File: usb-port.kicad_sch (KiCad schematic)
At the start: 6 parts, among them J3 USB_A

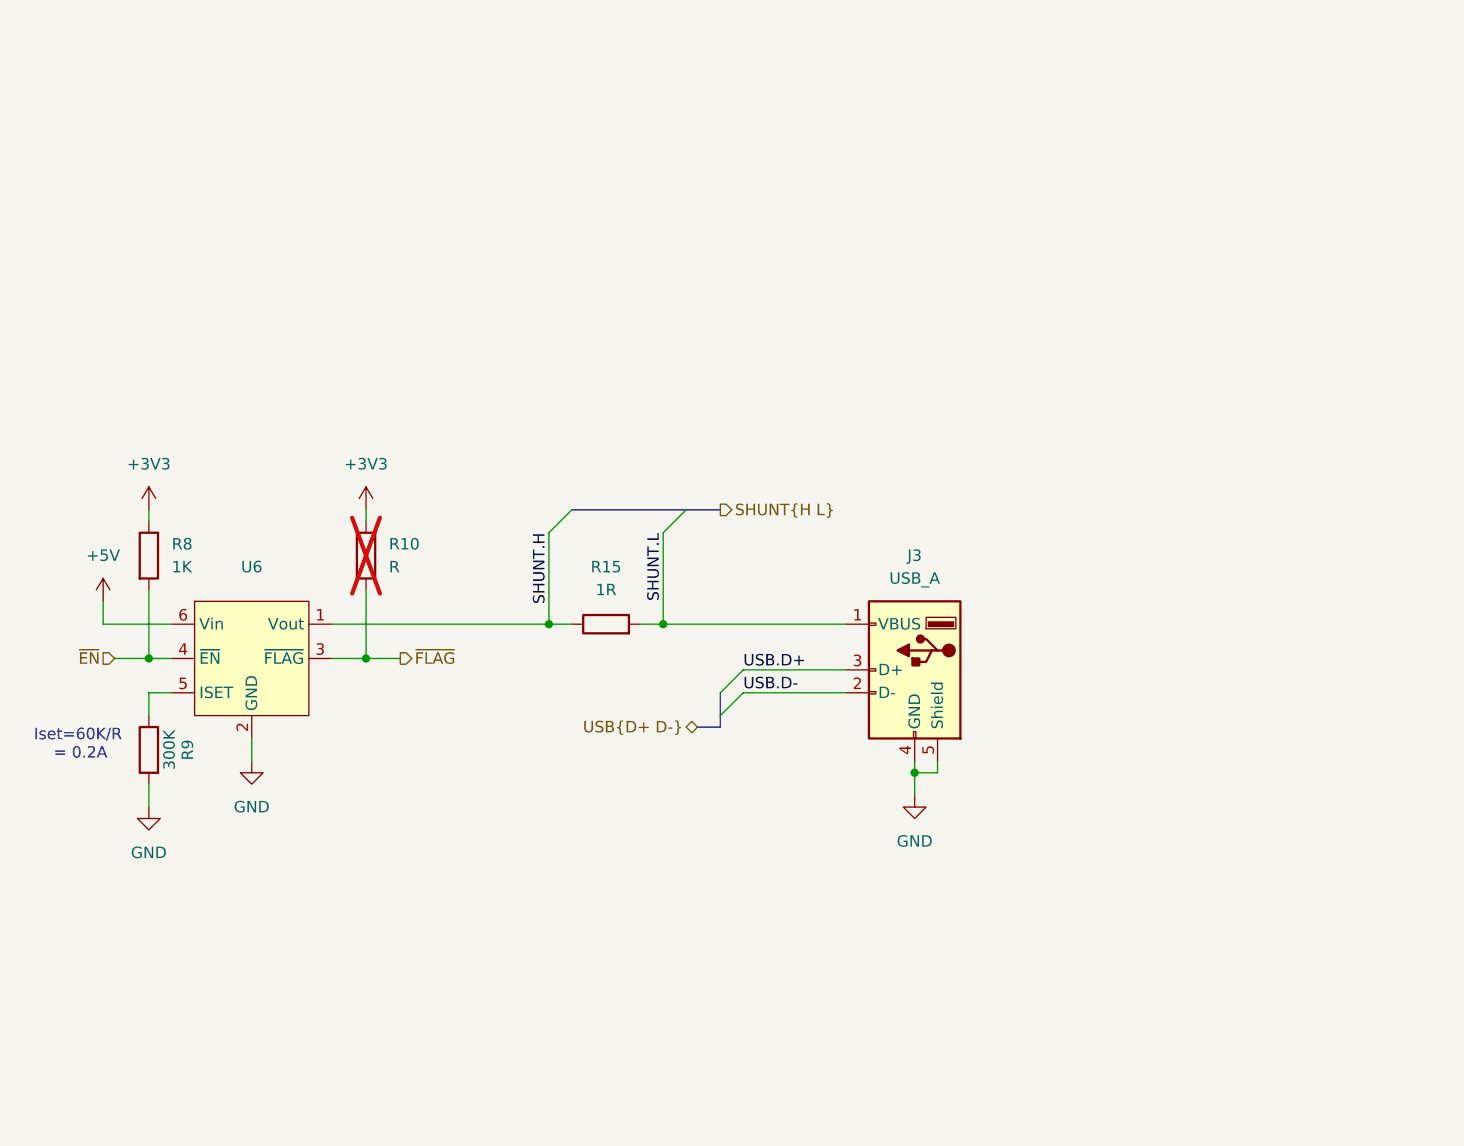
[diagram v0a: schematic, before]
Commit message: Add RP2350B from example
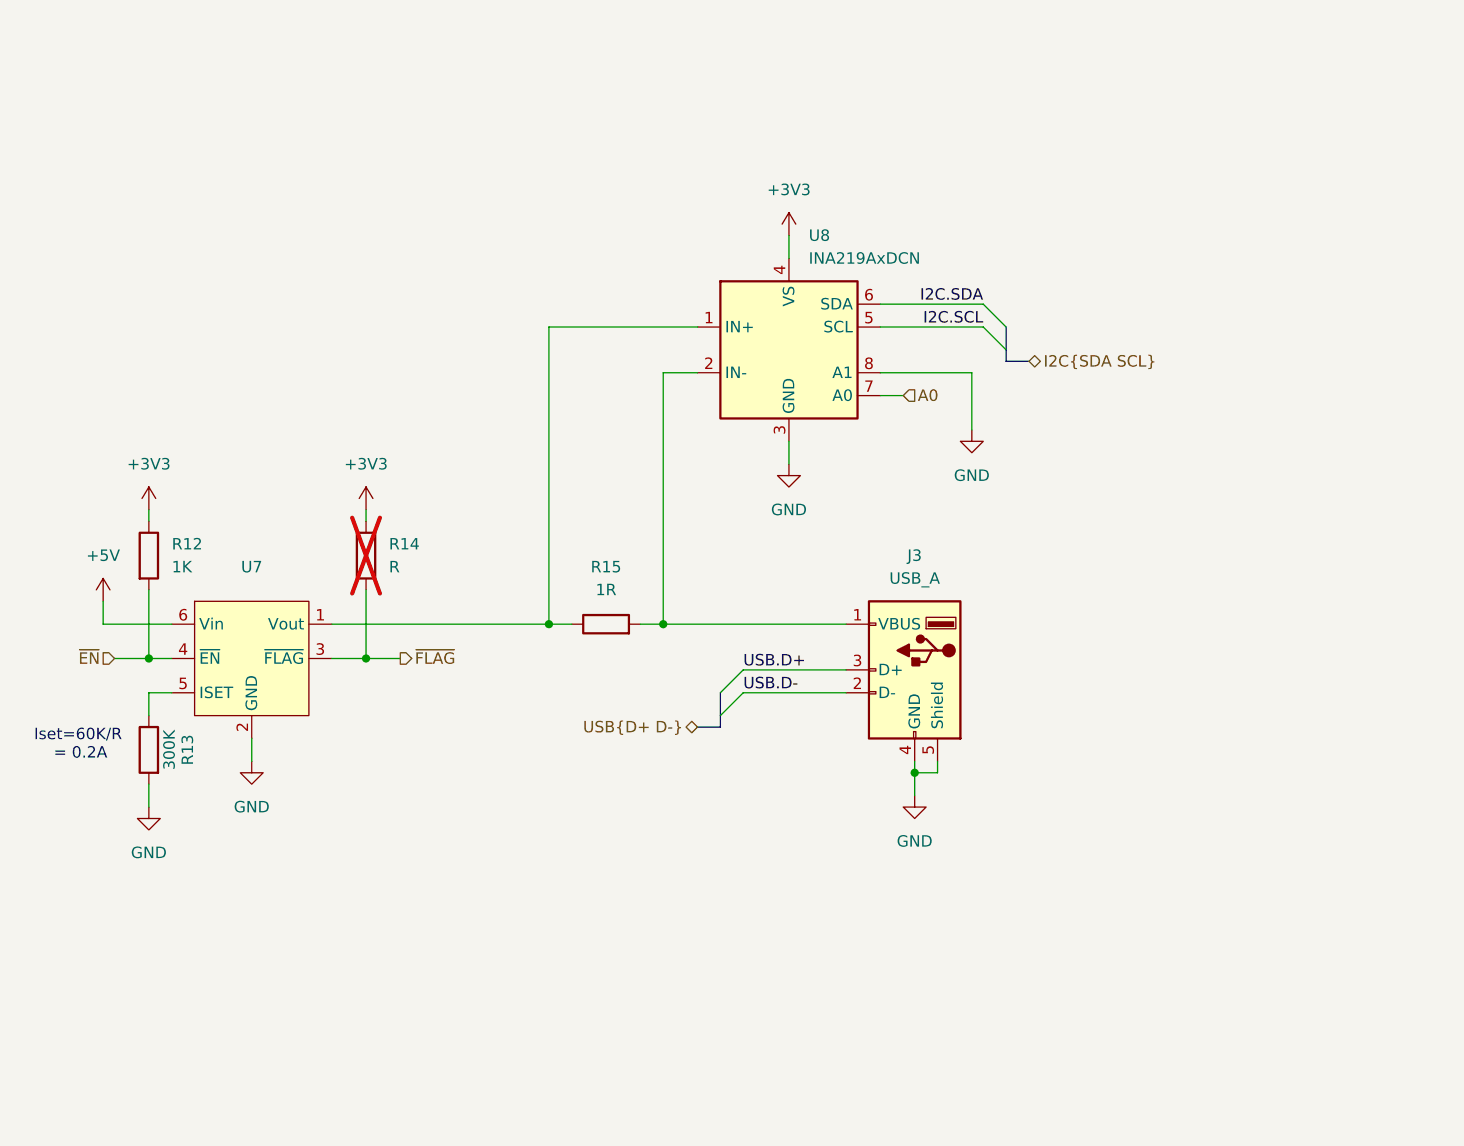
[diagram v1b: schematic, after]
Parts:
- added U8: INA219AxDCN, Package_TO_SOT_SMD:SOT-23-8, symbol Sensor_Energy:INA219AxDCN
- renumbered R8 to R12, R9 to R13, R10 to R14, U6 to U7
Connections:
- net +3V3: now also U8.4 (VS)
- net GND: now also U8.3 (GND), U8.8 (A1)
- net SHUNT.H: no longer names the net of R15.1, U7.1 (Vout)
- net SHUNT.H: now also U8.1 (IN+)
- net SHUNT.L: no longer names the net of J3.1 (VBUS), R15.2
- net SHUNT.L: now also U8.2 (IN-)
- new net A0: U8.7 (A0)
- new net I2C.SCL: U8.5 (SCL)
- new net I2C.SDA: U8.6 (SDA)

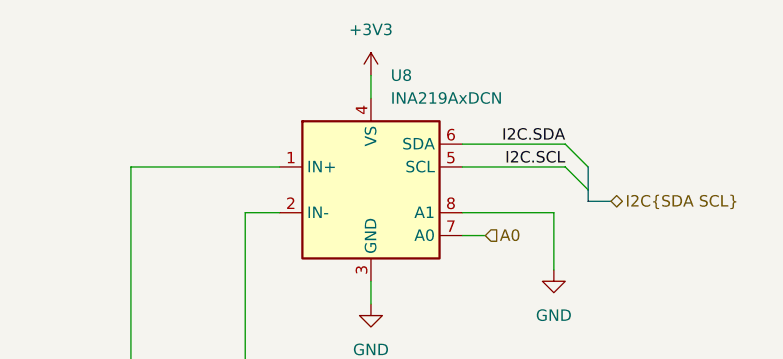
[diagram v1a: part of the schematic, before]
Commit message: Break out RP2350
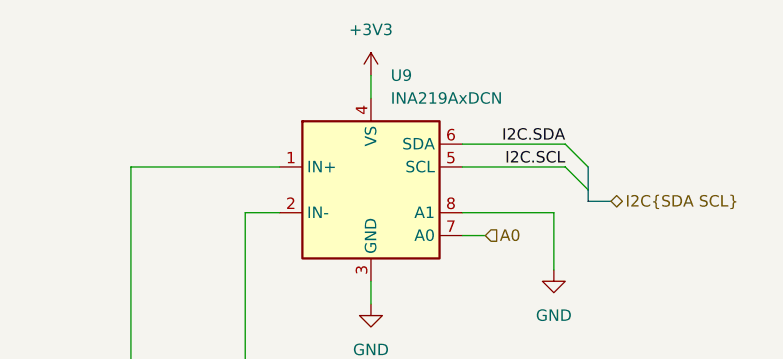
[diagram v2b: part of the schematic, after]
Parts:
- renumbered U8 to U9
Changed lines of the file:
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@@
 		(dnp no)
 		(fields_autoplaced yes)
-		(property "Reference" "#PWR34"
+		(property "Reference" "#PWR35"
 			(at 175.26 64.77 0)
 			(effects
@@
 		(dnp no)
 		(fields_autoplaced yes)
-		(property "Reference" "U8"
+		(property "Reference" "U9"
 			(at 157.1341 36.83 0)
 			(effects
@@
 		(dnp no)
 		(fields_autoplaced yes)
-		(property "Reference" "#PWR32"
+		(property "Reference" "#PWR33"
 			(at 154.94 40.64 0)
 			(effects
@@
 		(dnp no)
 		(fields_autoplaced yes)
-		(property "Reference" "#PWR30"
+		(property "Reference" "#PWR31"
 			(at 154.94 68.58 0)
 			(effects

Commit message: Start Layout
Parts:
- added C13: 100uF, Capacitor_SMD:C_1206_3216Metric, symbol Device:C
- added U10: SRV05-4, Package_TO_SOT_SMD:SOT-23-6, symbol Power_Protection:SRV05-4
- renumbered J3 to J2, R14 to R10, R15 to R11, R12 to R8, R13 to R9, U7 to U6, U9 to U8
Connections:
- net GND: now also C13.2, U10.2 (VN)
- net USB.D+: now also U10.3 (IO2)
- net USB.D-: now also U10.1 (IO1)
- net at J2.1 (VBUS), R11.2, U8.2 (IN-): now also C13.1, U10.5 (VP)
- no-connect marks 0 -> 2
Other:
- moved on the sheet: J2

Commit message: Layout Tester and USB Hub
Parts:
- added C58: 100nF, Capacitor_SMD:C_0402_1005Metric, symbol Device:C
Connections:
- net +3V3: now also C58.1
- net GND: now also C58.2
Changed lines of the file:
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@@
+	(wire
+		(pts
+			(xy 135.89 29.21) (xy 135.89 31.75)
+		)
+		(stroke
+			(width 0)
+			(type default)
+		)
+	)
 	(wire
 		(pts
 			(xy 128.27 80.01) (xy 130.81 80.01)
+		)
+		(stroke
+			(width 0)
+			(type default)
+		)
+	)
+	(wire
+		(pts
+			(xy 135.89 19.05) (xy 135.89 21.59)
 		)
 		(stroke
@@
 	)
 	(symbol
+		(lib_id "power:+3V3")
+		(at 135.89 19.05 0)
+		(unit 1)
+		(exclude_from_sim no)
+		(in_bom yes)
+		(on_board yes)
+		(dnp no)
+		(fields_autoplaced yes)
+		(property "Reference" "#PWR098"
+			(at 135.89 22.86 0)
+			(effects
+				(font
+					(size 1.27 1.27)
+				)
+				(hide yes)
+			)
+		)
+		(property "Value" "+3V3"
+			(at 135.89 13.97 0)
+			(effects
+				(font
+					(size 1.27 1.27)
+				)
+			)
+		)
+		(property "Footprint" ""
+			(at 135.89 19.05 0)
+			(effects
+				(font
+					(size 1.27 1.27)
+				)
+				(hide yes)
+			)
+		)
+		(property "Datasheet" ""
+			(at 135.89 19.05 0)
+			(effects
+				(font
+					(size 1.27 1.27)
+				)
+				(hide yes)
+			)
+		)
+		(property "Description" "Power symbol creates a global label with name \"+3V3\""
+			(at 135.89 19.05 0)
+			(effects
+				(font
+					(size 1.27 1.27)
+				)
+				(hide yes)
+			)
+		)
+		(pin "1"
+		)
+		(instances
+			(project "shield"
+				(path "/d57ea000-ef46-42c0-b86a-7e6b1d4431c2/47b780ba-46a2-431c-9095-9b4236a14243"
+					(reference "#PWR099")
+					(unit 1)
+				)
+				(path "/d57ea000-ef46-42c0-b86a-7e6b1d4431c2/fb2e97f4-c33b-4fcc-91cb-29a4dc5c2c3d"
+					(reference "#PWR098")
+					(unit 1)
+				)
+			)
+		)
+	)
+	(symbol
 		(lib_id "power:GND")
 		(at 175.26 58.42 0)
@@
 	)
 	(symbol
+		(lib_id "Device:C")
+		(at 135.89 25.4 0)
+		(unit 1)
+		(exclude_from_sim no)
+		(in_bom yes)
+		(on_board yes)
+		(dnp no)
+		(fields_autoplaced yes)
+		(property "Reference" "C58"
+			(at 139.7 24.1299 0)
+			(effects
+				(font
+					(size 1.27 1.27)
+				)
+				(justify left)
+			)
+		)
+		(property "Value" "100nF"
+			(at 139.7 26.6699 0)
+			(effects
+				(font
+					(size 1.27 1.27)
+				)
+				(justify left)
+			)
+		)
+		(property "Footprint" "Capacitor_SMD:C_0402_1005Metric"
+			(at 136.8552 29.21 0)
+			(effects
+				(font
+					(size 1.27 1.27)
+				)
+				(hide yes)
+			)
+		)
+		(property "Datasheet" "~"
+			(at 135.89 25.4 0)
+			(effects
+				(font
+					(size 1.27 1.27)
+				)
+				(hide yes)
+			)
+		)
+		(property "Description" "Unpolarized capacitor"
+			(at 135.89 25.4 0)
+			(effects
+				(font
+					(size 1.27 1.27)
+				)
+				(hide yes)
+			)
+		)
+		(property "LCSC" "C1525"
+			(at 135.89 25.4 0)
+			(effects
+				(font
+					(size 1.27 1.27)
+				)
+				(hide yes)
+			)
+		)
+		(pin "2"
+		)
+		(pin "1"
+		)
+		(instances
+			(project "shield"
+				(path "/d57ea000-ef46-42c0-b86a-7e6b1d4431c2/47b780ba-46a2-431c-9095-9b4236a14243"
+					(reference "C59")
+					(unit 1)
+				)
+				(path "/d57ea000-ef46-42c0-b86a-7e6b1d4431c2/fb2e97f4-c33b-4fcc-91cb-29a4dc5c2c3d"
+					(reference "C58")
+					(unit 1)
+				)
+			)
+		)
+	)
+	(symbol
 		(lib_id "power:+5V")
 		(at 78.74 77.47 0)
@@
 					(unit 1)
 				)
+			)
+		)
+	)
+	(symbol
+		(lib_id "power:GND")
+		(at 135.89 31.75 0)
+		(unit 1)
+		(exclude_from_sim no)
+		(in_bom yes)
+		(on_board yes)
+		(dnp no)
+		(fields_autoplaced yes)
+		(property "Reference" "#PWR0100"
+			(at 135.89 38.1 0)
+			(effects
+				(font
+					(size 1.27 1.27)
+				)
+				(hide yes)
+			)
+		)
+		(property "Value" "GND"
+			(at 135.89 36.83 0)
+			(effects
+				(font
+					(size 1.27 1.27)
+				)
+			)
+		)
+		(property "Footprint" ""
+			(at 135.89 31.75 0)
+			(effects
+				(font
+					(size 1.27 1.27)
+				)
+				(hide yes)
+			)
+		)
+		(property "Datasheet" ""
+			(at 135.89 31.75 0)
+			(effects
+				(font
+					(size 1.27 1.27)
+				)
+				(hide yes)
+			)
+		)
+		(property "Description" "Power symbol creates a global label with name \"GND\" , ground"
+			(at 135.89 31.75 0)
+			(effects
+				(font
+					(size 1.27 1.27)
+				)
+				(hide yes)
+			)
+		)
+		(pin "1"
+		)
+		(instances
+			(project "shield"
+				(path "/d57ea000-ef46-42c0-b86a-7e6b1d4431c2/47b780ba-46a2-431c-9095-9b4236a14243"
+					(reference "#PWR0101")
+					(unit 1)
+				)
+				(path "/d57ea000-ef46-42c0-b86a-7e6b1d4431c2/fb2e97f4-c33b-4fcc-91cb-29a4dc5c2c3d"
+					(reference "#PWR0100")
+					(unit 1)
+				)

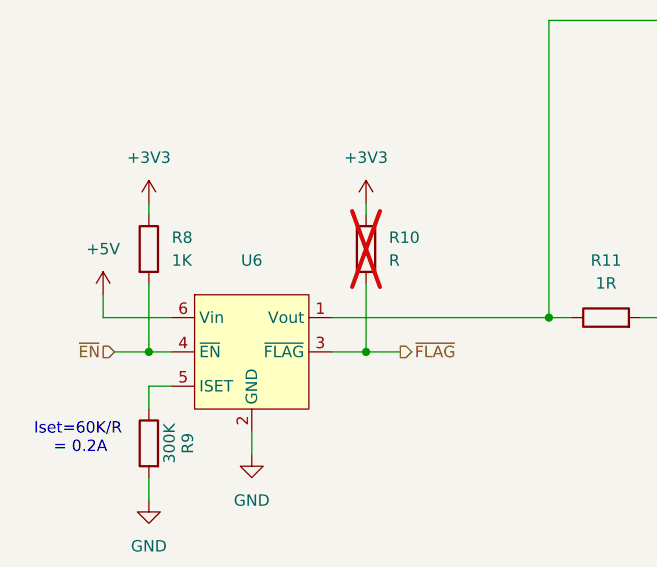
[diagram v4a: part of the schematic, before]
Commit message: JLC rotations
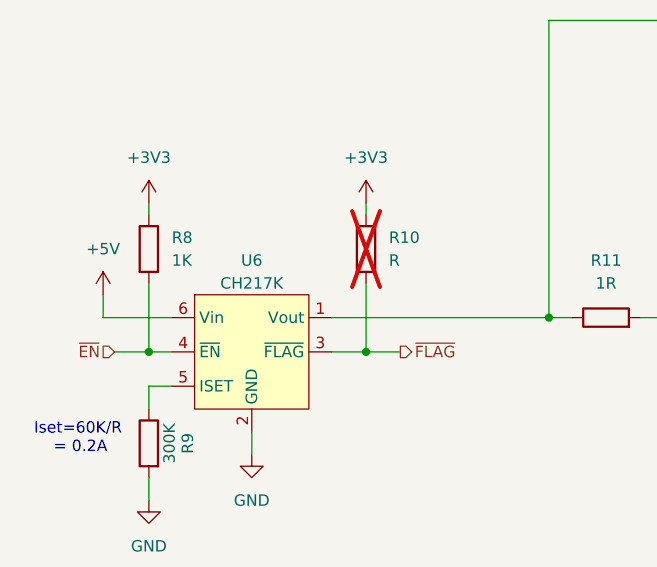
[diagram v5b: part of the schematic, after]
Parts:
- U10: FT Rotation Offset (none) -> 90
- U6: value ~ -> CH217K; FT Rotation Offset (none) -> 90
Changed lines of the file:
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@@
+			)
+		)
+		(property "FT Rotation Offset" ""
+			(at 83.82 72.39 0)
+			(effects
+				(font
+					(size 1.27 1.27)
+				)
+				(hide yes)
 			)
 		)
@@
 			)
 		)
+		(property "FT Rotation Offset" ""
+			(at 83.82 93.98 90)
+			(effects
+				(font
+					(size 1.27 1.27)
+				)
+				(hide yes)
+			)
+		)
 		(pin "1"
 		)
@@
 			)
 		)
+		(property "FT Rotation Offset" ""
+			(at 148.59 90.17 0)
+			(effects
+				(font
+					(size 1.27 1.27)
+				)
+				(hide yes)
+			)
+		)
 		(pin "1"
 		)
@@
 			)
 		)
-		(property "Value" "~"
+		(property "Value" "CH217K"
 			(at 95.25 76.2 0)
 			(effects
@@
 			)
 		)
+		(property "FT Rotation Offset" "90"
+			(at 95.25 83.82 0)
+			(effects
+				(font
+					(size 1.27 1.27)
+				)
+				(hide yes)
+			)
+		)
 		(pin "3"
 		)
@@
 		)
 		(property "LCSC" "C7420376"
+			(at 214.63 114.3 0)
+			(effects
+				(font
+					(size 1.27 1.27)
+				)
+				(hide yes)
+			)
+		)
+		(property "FT Rotation Offset" "90"
 			(at 214.63 114.3 0)
 			(effects
@@
 			)
 		)
+		(property "FT Rotation Offset" ""
+			(at 200.66 85.09 0)
+			(effects
+				(font
+					(size 1.27 1.27)
+				)
+				(hide yes)
+			)
+		)
 		(pin "1"
 		)
@@
 			)
 		)
+		(property "FT Rotation Offset" ""
+			(at 154.94 49.53 0)
+			(effects
+				(font
+					(size 1.27 1.27)
+				)
+				(hide yes)
+			)
+		)
 		(pin "6"
 		)
@@
 			)
 		)
+		(property "FT Rotation Offset" ""
+			(at 135.89 25.4 0)
+			(effects
+				(font
+					(size 1.27 1.27)
+				)
+				(hide yes)
+			)
+		)
 		(pin "2"
 		)
@@
 			)
 		)
+		(property "FT Rotation Offset" ""
+			(at 107.95 72.39 0)
+			(effects
+				(font
+					(size 1.27 1.27)
+				)
+				(hide yes)
+			)
+		)
 		(pin "1"
 		)
@@
 			(at 134.62 80.01 90)
 			(effects
+				(font
+					(size 1.27 1.27)
+				)
+				(hide yes)
+			)
+		)
+		(property "FT Rotation Offset" ""
+			(at 134.62 80.01 90)
+			(effects
